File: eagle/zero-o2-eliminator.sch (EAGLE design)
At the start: 8 parts, among them U1 TINY85-20-DIP

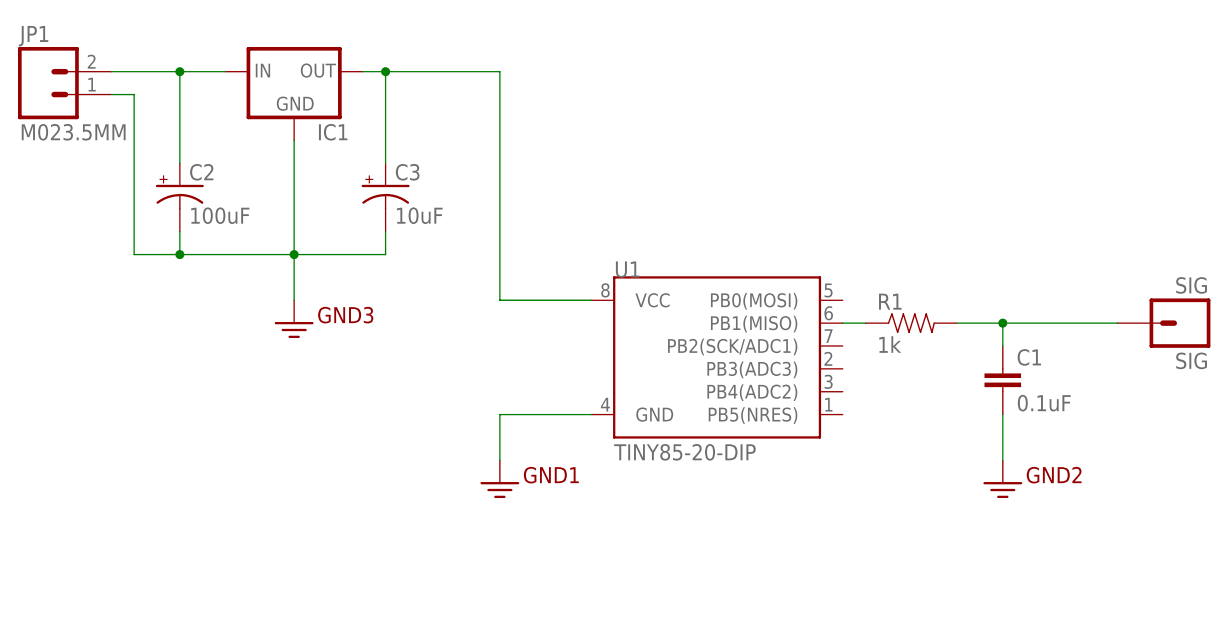
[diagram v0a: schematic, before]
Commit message: created initial board
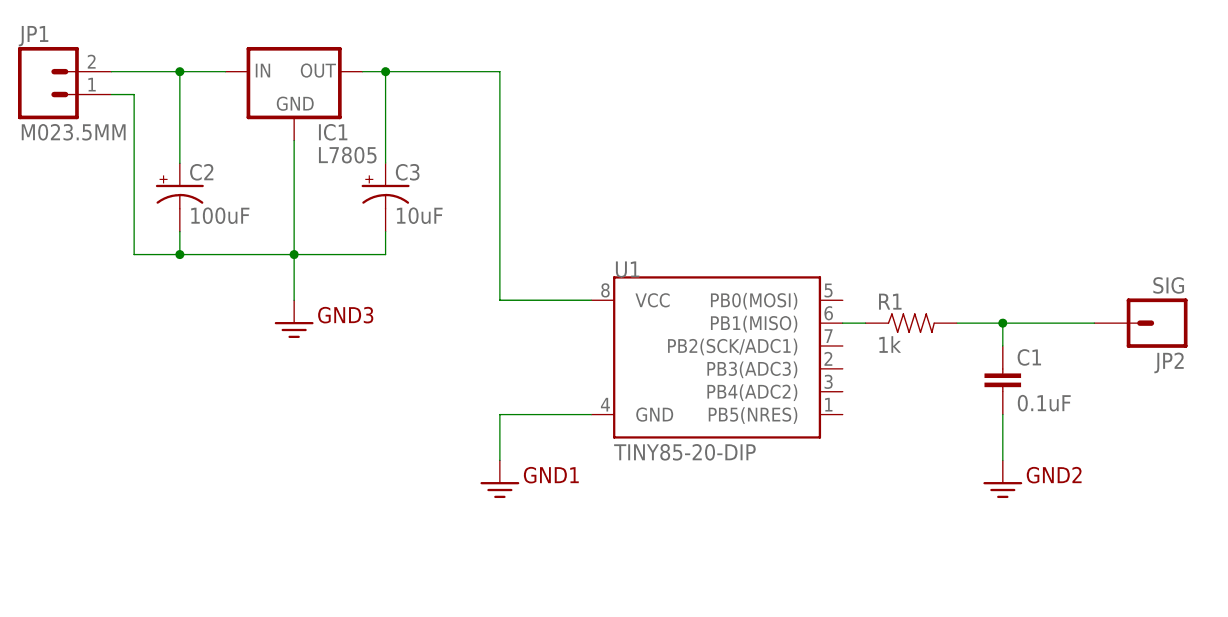
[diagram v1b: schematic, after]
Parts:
- removed SIG: SIG, SparkFun-Connectors:M01PTH_LONGPAD
- added JP2: SIG, SparkFun-Connectors:M01PTH_LONGPAD
- IC1: value (none) -> L7805
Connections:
- net N$2: now also JP2.1; no longer SIG.1
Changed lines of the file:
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@@
 <part name="C1" library="SparkFun-Capacitors" deviceset="0.1UF-50V-20%(PTH)" device="KIT-EZ" value="0.1uF"/>
 <part name="GND2" library="SparkFun-Aesthetics" deviceset="GND2" device=""/>
-<part name="SIG" library="SparkFun-Connectors" deviceset="M01" device="PTH_LONGPAD" value="SIG"/>
-<part name="IC1" library="SparkFun-PowerIC" deviceset="V_REG_78XX" device="SIDE"/>
+<part name="IC1" library="SparkFun-PowerIC" deviceset="V_REG_78XX" device="SIDE" value="L7805"/>
 <part name="C2" library="SparkFun-Capacitors" deviceset="10UF-25V-20%(PTH)" device="KIT" value="100uF"/>
 <part name="C3" library="SparkFun-Capacitors" deviceset="10UF-25V-20%(PTH)" device="KIT" value="10uF"/>
 <part name="GND3" library="SparkFun-Aesthetics" deviceset="GND2" device=""/>
 <part name="JP1" library="SparkFun-Connectors" deviceset="M02" device="3.5MM"/>
+<part name="JP2" library="SparkFun-Connectors" deviceset="M01" device="PTH_LONGPAD" value="SIG"/>
 </parts>
 <sheets>
@@
 <instance part="C1" gate="G$1" x="78.74" y="43.18"/>
 <instance part="GND2" gate="G$1" x="78.74" y="33.02"/>
-<instance part="SIG" gate="G$1" x="99.06" y="50.8" rot="R180"/>
 <instance part="IC1" gate="G$1" x="0" y="78.74"/>
 <instance part="C2" gate="G$1" x="-12.7" y="66.04"/>
@@
 <instance part="GND3" gate="G$1" x="0" y="50.8"/>
 <instance part="JP1" gate="G$1" x="-27.94" y="76.2"/>
+<instance part="JP2" gate="G$1" x="96.52" y="50.8" rot="R180"/>
 </instances>
 <busses>
@@
 <pinref part="C1" gate="G$1" pin="1"/>
 <wire x1="78.74" y1="50.8" x2="78.74" y2="48.26" width="0.1524" layer="91"/>
-<pinref part="SIG" gate="G$1" pin="1"/>
-<wire x1="78.74" y1="50.8" x2="91.44" y2="50.8" width="0.1524" layer="91"/>
+<wire x1="78.74" y1="50.8" x2="88.9" y2="50.8" width="0.1524" layer="91"/>
 <junction x="78.74" y="50.8"/>
+<pinref part="JP2" gate="G$1" pin="1"/>
 </segment>
 </net>

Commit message: latest
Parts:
- removed JP1: M023.5MM, SparkFun-Connectors:M023.5MM
- removed JP2: SIG, SparkFun-Connectors:M01PTH_LONGPAD
- added JP3: (no value), SparkFun-Connectors:M03SCREW
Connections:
- removed net 3.3V: C1.2, C2.-, C3.-, IC1.GND, JP1.1, U1.GND
- removed net N$2: C1.1, JP2.1, R1.2
- removed net N$3: C2.+, IC1.IN, JP1.2
- new net 12V: C2.+, IC1.IN, JP3.3
- new net GND: C1.2, C2.-, C3.-, IC1.GND, JP3.2, U1.GND
- new net OUT: C1.1, JP3.1, R1.2
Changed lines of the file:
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@@
 <part name="C3" library="SparkFun-Capacitors" deviceset="10UF-25V-20%(PTH)" device="KIT" value="10uF"/>
 <part name="GND3" library="SparkFun-Aesthetics" deviceset="GND2" device=""/>
-<part name="JP1" library="SparkFun-Connectors" deviceset="M02" device="3.5MM"/>
-<part name="JP2" library="SparkFun-Connectors" deviceset="M01" device="PTH_LONGPAD" value="SIG"/>
+<part name="JP3" library="SparkFun-Connectors" deviceset="M03" device="SCREW"/>
 </parts>
 <sheets>
@@
 <instance part="C3" gate="G$1" x="10.16" y="66.04"/>
 <instance part="GND3" gate="G$1" x="0" y="50.8"/>
-<instance part="JP1" gate="G$1" x="-27.94" y="76.2"/>
-<instance part="JP2" gate="G$1" x="96.52" y="50.8" rot="R180"/>
+<instance part="JP3" gate="G$1" x="-22.86" y="25.4"/>
 </instances>
 <busses>
 </busses>
 <nets>
-<net name="3.3V" class="0">
+<net name="GND" class="0">
 <segment>
 <pinref part="GND1" gate="G$1" pin="3.3V"/>
@@
 <pinref part="IC1" gate="G$1" pin="GND"/>
 <wire x1="0" y1="71.12" x2="0" y2="58.42" width="0.1524" layer="91"/>
-<pinref part="JP1" gate="G$1" pin="1"/>
 <wire x1="-20.32" y1="76.2" x2="-17.78" y2="76.2" width="0.1524" layer="91"/>
 <wire x1="-17.78" y1="76.2" x2="-17.78" y2="58.42" width="0.1524" layer="91"/>
 <wire x1="-17.78" y1="58.42" x2="-12.7" y2="58.42" width="0.1524" layer="91"/>
 <junction x="-12.7" y="58.42"/>
+<label x="-22.86" y="73.66" size="1.778" layer="95"/>
+</segment>
+<segment>
+<pinref part="JP3" gate="G$1" pin="2"/>
+<wire x1="-15.24" y1="25.4" x2="-5.08" y2="25.4" width="0.1524" layer="91"/>
+<label x="-5.08" y="25.4" size="1.778" layer="95"/>
 </segment>
 </net>
@@
 </segment>
 </net>
-<net name="N$2" class="0">
+<net name="OUT" class="0">
 <segment>
 <pinref part="R1" gate="G$1" pin="2"/>
@@
 <wire x1="78.74" y1="50.8" x2="88.9" y2="50.8" width="0.1524" layer="91"/>
 <junction x="78.74" y="50.8"/>
-<pinref part="JP2" gate="G$1" pin="1"/>
+<label x="88.9" y="50.8" size="1.778" layer="95"/>
+</segment>
+<segment>
+<pinref part="JP3" gate="G$1" pin="1"/>
+<wire x1="-15.24" y1="22.86" x2="-5.08" y2="22.86" width="0.1524" layer="91"/>
+<label x="-5.08" y="22.86" size="1.778" layer="95"/>
 </segment>
 </net>
-<net name="N$3" class="0">
+<net name="12V" class="0">
 <segment>
 <pinref part="IC1" gate="G$1" pin="IN"/>
@@
 <pinref part="C2" gate="G$1" pin="+"/>
 <wire x1="-12.7" y1="78.74" x2="-12.7" y2="68.58" width="0.1524" layer="91"/>
-<pinref part="JP1" gate="G$1" pin="2"/>
 <wire x1="-20.32" y1="78.74" x2="-12.7" y2="78.74" width="0.1524" layer="91"/>
 <junction x="-12.7" y="78.74"/>
+<label x="-20.32" y="78.74" size="1.778" layer="95"/>
+</segment>
+<segment>
+<pinref part="JP3" gate="G$1" pin="3"/>
+<wire x1="-15.24" y1="27.94" x2="-5.08" y2="27.94" width="0.1524" layer="91"/>
+<label x="-5.08" y="27.94" size="1.778" layer="95"/>
 </segment>
 </net>
